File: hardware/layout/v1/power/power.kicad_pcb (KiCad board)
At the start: 4 copper layers, 28.5 x 21.5 mm, 40 parts, among them J1 Main board, U1 TPS54360DDAR, U2 TPS54360DDAR, U3 AP2112K-3.3

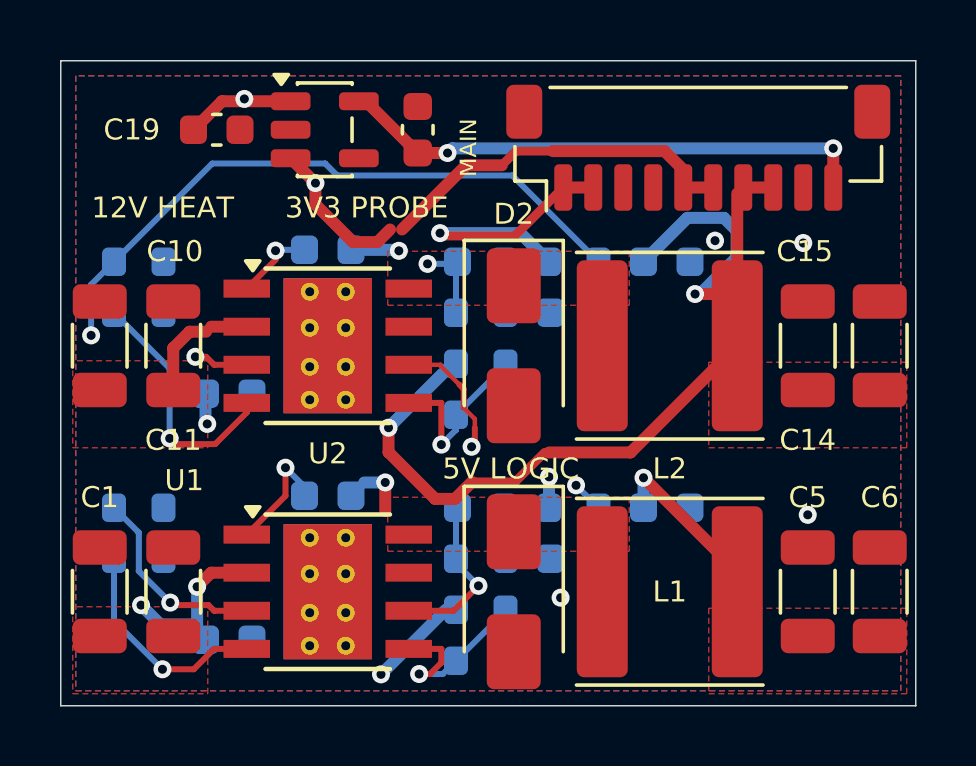
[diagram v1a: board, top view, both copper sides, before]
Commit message: Update dome PCB layout with manual reference and label placement, add Stock_Optional field for LTR-390UV-01 sensor to allow JLC assembly when in stock without failing release on shortage
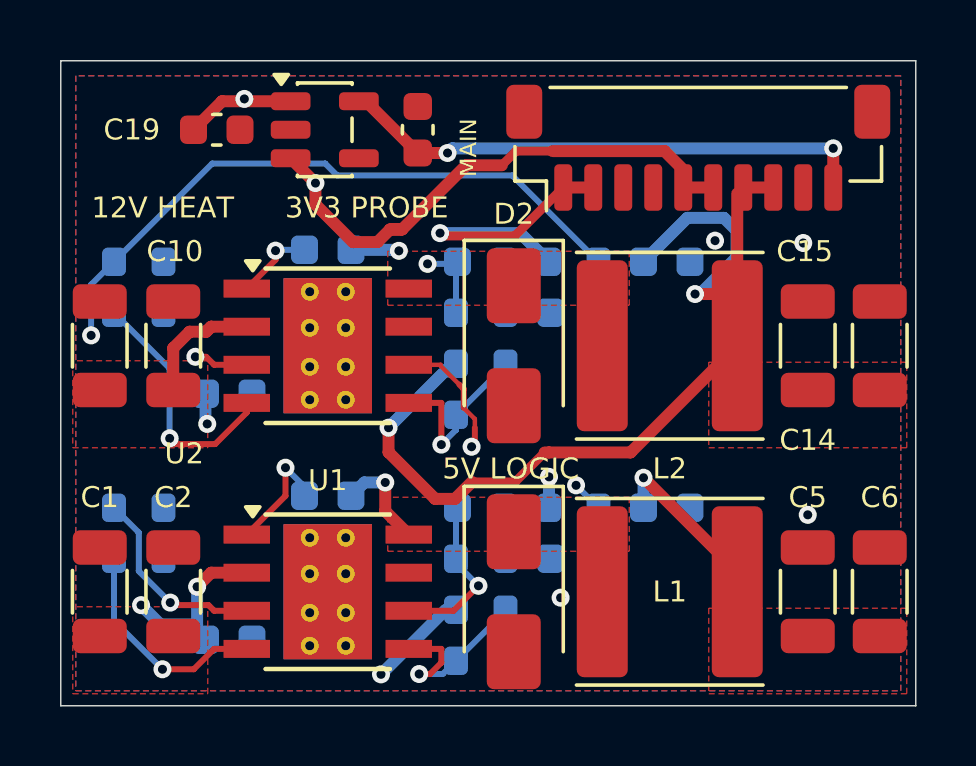
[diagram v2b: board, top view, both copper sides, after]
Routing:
- net LOGIC_SW: track 1.65 -> 3.39 mm
- net +5V: track 59.6 -> 60.8 mm
- net VIN_PROT: track 47.0 -> 47.9 mm
